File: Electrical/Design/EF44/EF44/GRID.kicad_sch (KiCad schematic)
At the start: 9 parts, among them J10 TE Connectivity 84982-8, J11 TE Connectivity 84982-8, J4 TE Connectivity 84982-8, J5 TE Connectivity 84982-8, J6 TE Connectivity 84982-8, J7 TE Connectivity 84982-8, J8 TE Connectivity 84982-8, J9 TE Connectivity 84982-8, M1 (NF)

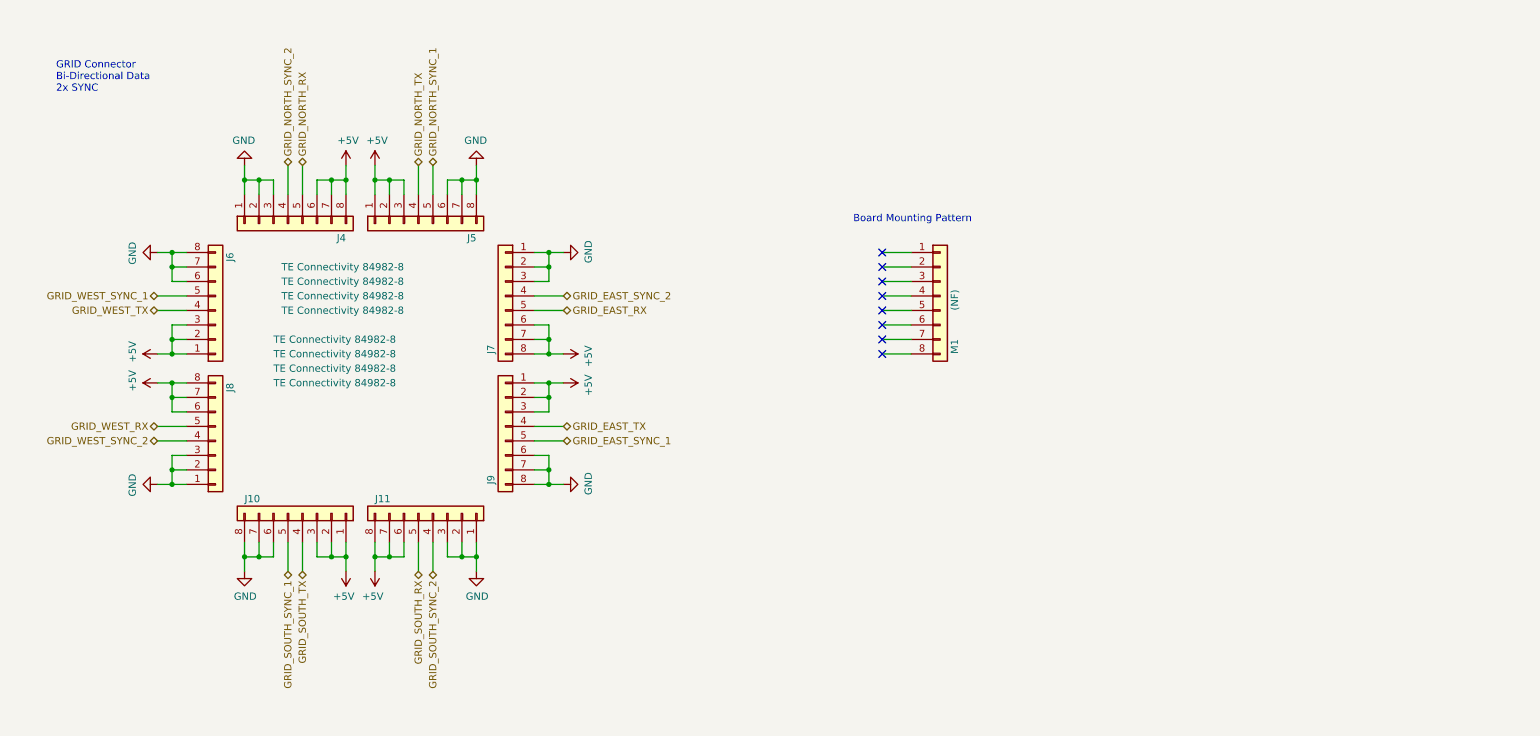
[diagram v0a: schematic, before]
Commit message: SUKU EF44 created from EN16 Base
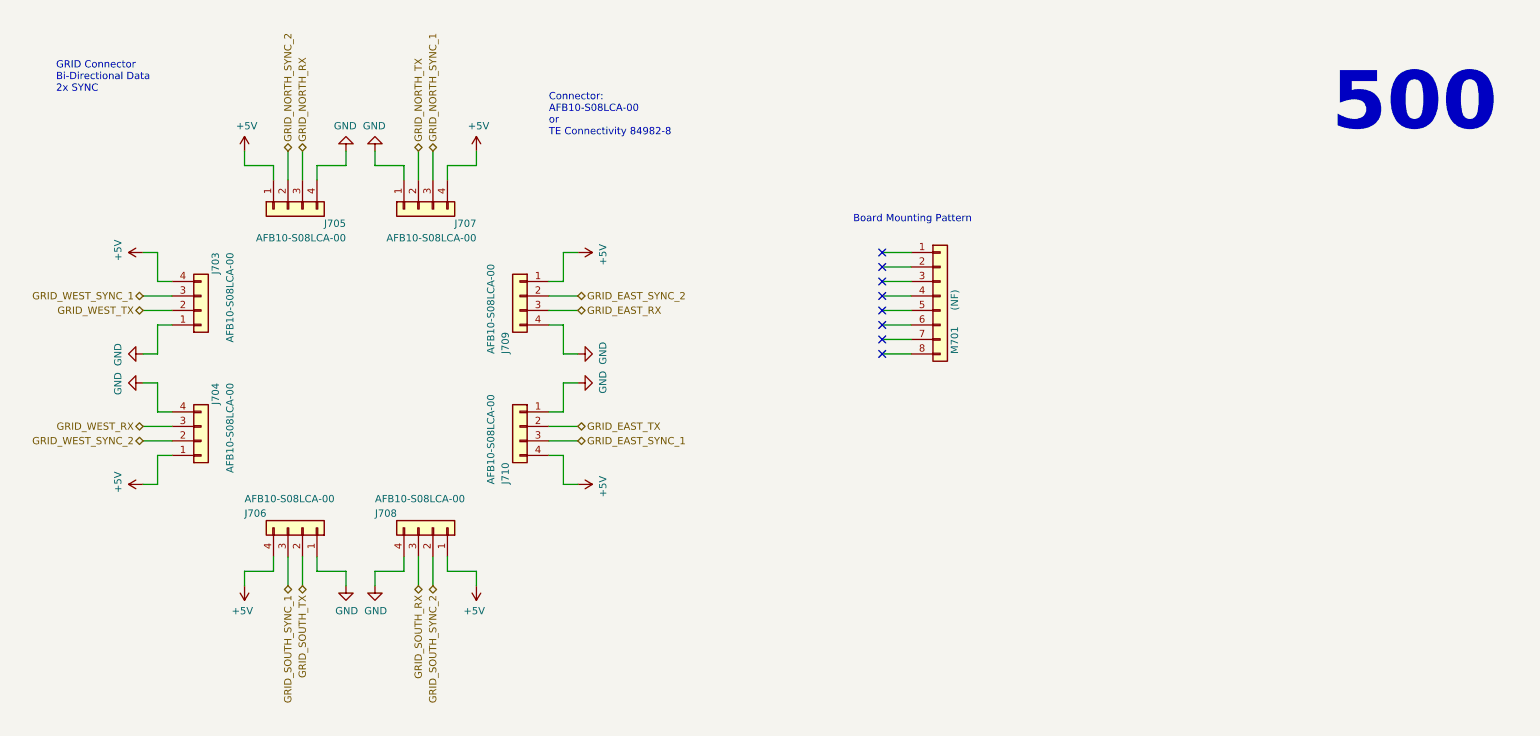
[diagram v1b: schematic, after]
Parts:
- removed J10, J11, J4, J5, J6, J7, J8, J9: TE Connectivity 84982-8, suku_basics:grid_ffc_8_vertical_smd, symbol Connector_Generic:Conn_01x08
- added J703, J704, J705, J706, J707, J708, J709, J710: AFB10-S08LCA-00, suku_basics:J_INTERFACE_SPRINGPATTERN, symbol Connector_Generic:Conn_01x04
- renumbered M1 to M701
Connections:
- net +5V: now also J703.4 (Pin_4), J704.1 (Pin_1), J705.1 (Pin_1), J706.4 (Pin_4), J707.4 (Pin_4), J708.1 (Pin_1), J709.1 (Pin_1), J710.4 (Pin_4)
- net GND: now also J703.1 (Pin_1), J704.4 (Pin_4), J705.4 (Pin_4), J706.1 (Pin_1), J707.1 (Pin_1), J708.4 (Pin_4), J709.4 (Pin_4), J710.1 (Pin_1)
- net GRID_EAST_RX: now also J709.3 (Pin_3)
- net GRID_EAST_SYNC_1: now also J710.3 (Pin_3)
- net GRID_EAST_SYNC_2: now also J709.2 (Pin_2)
- net GRID_EAST_TX: now also J710.2 (Pin_2)
- net GRID_NORTH_RX: now also J705.3 (Pin_3)
- net GRID_NORTH_SYNC_1: now also J707.3 (Pin_3)
- net GRID_NORTH_SYNC_2: now also J705.2 (Pin_2)
- net GRID_NORTH_TX: now also J707.2 (Pin_2)
- net GRID_SOUTH_RX: now also J708.3 (Pin_3)
- net GRID_SOUTH_SYNC_1: now also J706.3 (Pin_3)
- net GRID_SOUTH_SYNC_2: now also J708.2 (Pin_2)
- net GRID_SOUTH_TX: now also J706.2 (Pin_2)
- net GRID_WEST_RX: now also J704.3 (Pin_3)
- net GRID_WEST_SYNC_1: now also J703.3 (Pin_3)
- net GRID_WEST_SYNC_2: now also J704.2 (Pin_2)
- net GRID_WEST_TX: now also J703.2 (Pin_2)
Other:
- note added: "500"
- note added: "Connector: AFB10-S08LCA-00 or TE Connectivity 84982-8"
